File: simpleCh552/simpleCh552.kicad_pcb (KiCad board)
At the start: 2 copper layers, 20 x 27 mm, 15 parts, among them J1 Conn_01x02_Pin, J2 left, J3 Conn_01x03_Pin, SW1 SW_SPST, U1 CH552G

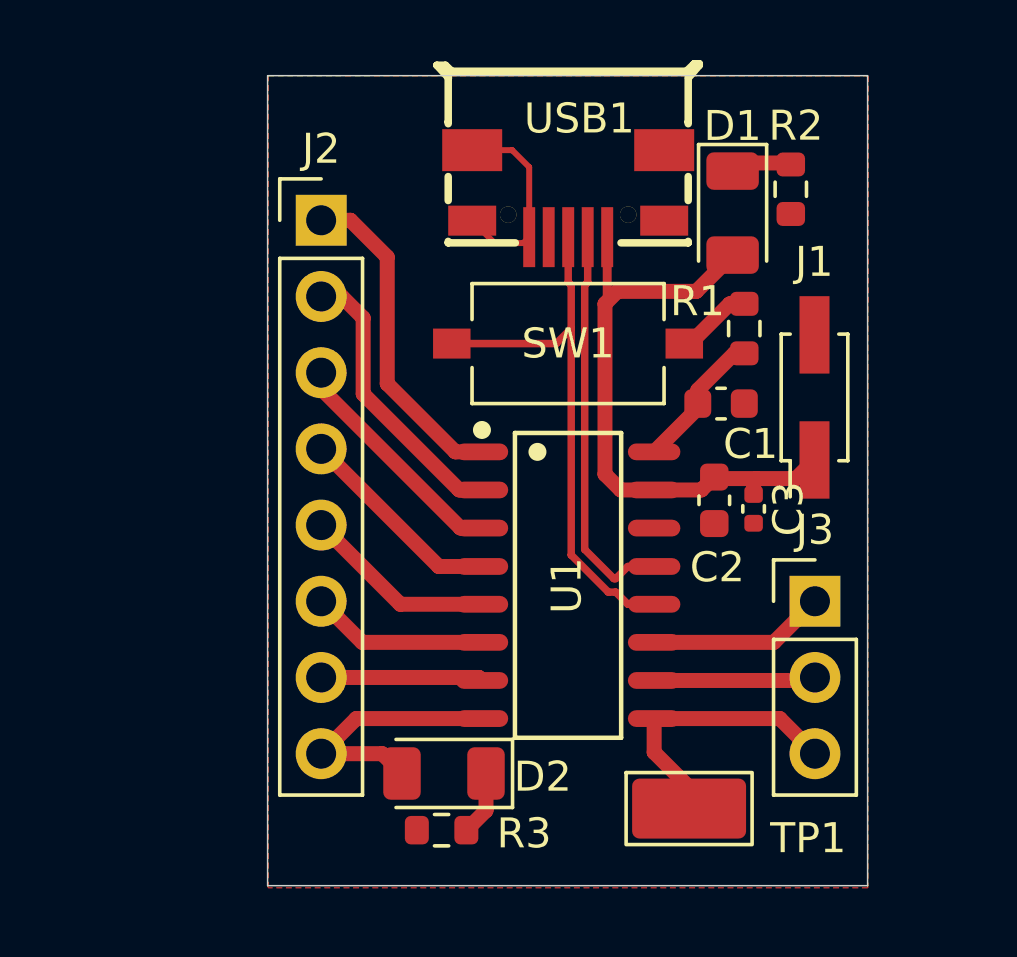
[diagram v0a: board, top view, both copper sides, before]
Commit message: Updated with MicroUSB link
Microsub board ready V1
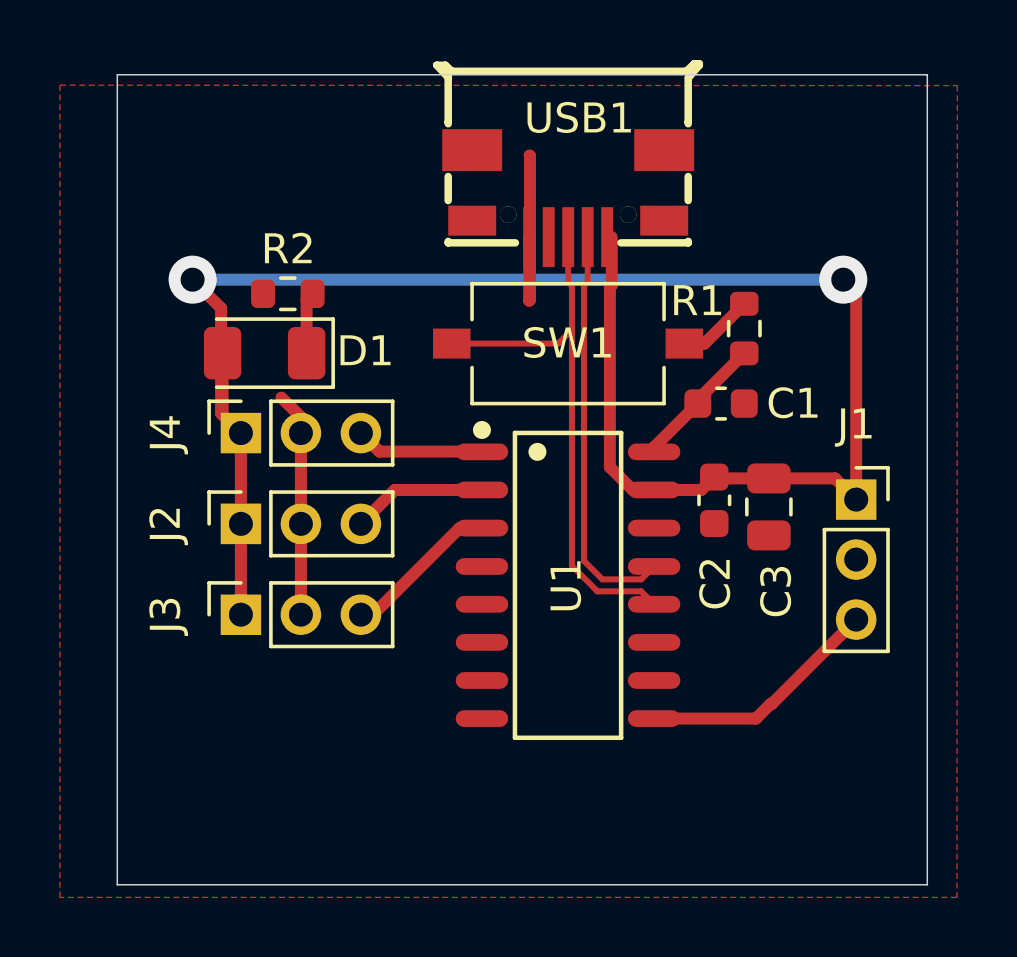
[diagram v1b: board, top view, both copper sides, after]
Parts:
- removed D2: LED, LED_SMD:LED_1206_3216Metric
- removed R3: 1k, Resistor_SMD:R_0603_1608Metric
- removed TP1: TestPoint, TestPoint:TestPoint_Keystone_5019_Miniature
- added J4: A3, Connector_PinSocket_2.00mm:PinSocket_1x03_P2.00mm_Vertical, F.Cu at (132.2, 60.0)
- C3: value 100n -> 10uf; footprint Capacitor_SMD:C_0402_1005Metric -> Capacitor_SMD:C_0805_2012Metric
- J1: value Conn_01x02_Pin -> A0; footprint Connector_PinHeader_2.00mm:PinHeader_2x01_P2.00mm_Vertical_SMD -> Connector_PinSocket_2.00mm:PinSocket_1x03_P2.00mm_Vertical
- J2: value left -> A1; footprint Connector_PinHeader_2.54mm:PinHeader_1x08_P2.54mm_Vertical -> Connector_PinSocket_2.00mm:PinSocket_1x03_P2.00mm_Vertical
- J3: value Conn_01x03_Pin -> A2; footprint Connector_PinHeader_2.54mm:PinHeader_1x03_P2.54mm_Vertical -> Connector_PinSocket_2.00mm:PinSocket_1x03_P2.00mm_Vertical
- moved J3 19.1 mm to (132.2, 66.0), turned to 90 degrees
- moved R2 17.1 mm to (133.8, 55.3), turned to 180 degrees
- moved D1 16.3 mm to (133.0, 57.3), turned to 180 degrees
- moved J2 10.5 mm to (132.2, 63.0), turned to 90 degrees
- moved J1 3.68 mm to (152.7, 62.2), turned to 0 degrees
- moved C3 0.51 mm to (149.8, 62.4)
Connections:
- J2 pad 1: Net-(J2-Pin_1) -> VCC
- J2 pad 2: Net-(J2-Pin_2) -> GND
- J2 pad 3: Net-(J2-Pin_3) -> A1
- J3 pad 1: /3.4 -> VCC
- J3 pad 2: /3.2 -> GND
- J3 pad 3: /1.1 -> A2
- U1 pad 1: Net-(J2-Pin_1) -> A3
- U1 pad 2: Net-(J2-Pin_2) -> A1
- U1 pad 3: Net-(J2-Pin_3) -> A2
- U1 pad 4: Net-(J2-Pin_4) -> unconnected-(U1-P1.6/MISO/RXD1/TIN4-Pad4)
- U1 pad 5: Net-(J2-Pin_5) -> unconnected-(U1-P1.7/SCK/TXD1/TIN5-Pad5)
- U1 pad 6: Net-(J2-Pin_6) -> unconnected-(U1-RST/T2EX_/CAP2_-Pad6)
- U1 pad 7: Net-(J2-Pin_7) -> unconnected-(U1-P3.1/PWM2_/TXD-Pad7)
- U1 pad 8: /3.0 -> unconnected-(U1-P3.0/PWM1_/RXD-Pad8)
- U1 pad 9: /1.1 -> A0
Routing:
- net VCC: track 21.1 -> 60.7 mm, vias 0 -> 2
- net Net-(J2-Pin_1): track 11.0 -> 0.00 mm
- net Net-(J2-Pin_2): track 9.51 -> 0.00 mm
- net /1.1: track 9.33 -> 0.00 mm
- net /3.0: track 8.81 -> 0.00 mm
- net A0: track 0.00 -> 8.10 mm
- net GND: track 6.76 -> 14.6 mm
- net Net-(J2-Pin_3): track 7.82 -> 0.00 mm
- net Net-(J2-Pin_4): track 6.98 -> 0.00 mm
- net Net-(J2-Pin_5): track 6.45 -> 0.00 mm
- net Net-(J2-Pin_6): track 5.93 -> 0.00 mm
- net /3.4: track 5.93 -> 0.00 mm
- net Net-(J2-Pin_7): track 5.40 -> 0.00 mm
- net /3.2: track 5.40 -> 0.00 mm
- net A2: track 0.00 -> 5.23 mm
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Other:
- board size 20 x 27 mm -> 27 x 27 mm

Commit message: update
update
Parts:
- removed USB1: MICROQTJ, mylib:MICRO-USB-SMD_MICROQTJ-5P
- added H1: MountingHole, MountingHole:MountingHole_2.1mm, F.Cu at (152.1, 51.3)
- added J5: Conn_01x04, Connector_PinSocket_2.54mm:PinSocket_1x04_P2.54mm_Vertical, F.Cu at (145.9, 52.3)
- R1, R2: footprint Resistor_SMD:R_0603_1608Metric -> Resistor_SMD:R_1206_3216Metric
- moved D1 1.18 mm to (134.2, 57.2)
- moved SW1 1.14 mm to (142.0, 57.1)
- moved R1 0.61 mm to (149.2, 55.9)
- moved R2 0.59 mm to (134.2, 54.9)
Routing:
- net GND: track 14.6 -> 8.51 mm
- net VCC: track 60.7 -> 55.4 mm, vias 2 -> 0
- net /D+: track 18.5 -> 22.0 mm
- net Net-(SW1-B): track 2.55 -> 5.40 mm
- net /D-: track 13.6 -> 15.6 mm
- net +3V3: track 4.53 -> 5.29 mm
- net A0: track 8.10 -> 8.76 mm
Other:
- board text added: "ch552Deej - Ved"

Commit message: update
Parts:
- removed H1: MountingHole, MountingHole:MountingHole_2.1mm
- removed the J1 at (152.7, 62.2)
- J2: value A1 -> Conn_01x04; footprint Connector_PinSocket_2.00mm:PinSocket_1x03_P2.00mm_Vertical -> Connector_Wire:SolderWire-0.5sqmm_1x04_P4.6mm_D0.9mm_OD2.1mm
- J3: value A2 -> Conn_01x04; footprint Connector_PinSocket_2.00mm:PinSocket_1x03_P2.00mm_Vertical -> Connector_Wire:SolderWire-0.5sqmm_1x04_P4.6mm_D0.9mm_OD2.1mm
- J4: value A3 -> Conn_01x04; footprint Connector_PinSocket_2.00mm:PinSocket_1x03_P2.00mm_Vertical -> Connector_Wire:SolderWire-0.5sqmm_1x04_P4.6mm_D0.9mm_OD2.1mm
- moved R1 23.4 mm to (149.0, 73.0), turned to -90 degrees
- moved J4 22.0 mm to (153.5, 65.5)
- moved D1 18.4 mm to (149.0, 68.1), turned to 90 degrees
- moved J2 15.4 mm to (143.0, 74.0), turned to 180 degrees
- moved J3 2.71 mm to (129.6, 65.5)
- moved J1 1.10 mm to (146.9, 51.8)
- moved C1 1.00 mm to (148.9, 59.7)
- moved R2 0.65 mm to (148.6, 56.1)
- moved C3 0.62 mm to (150.4, 62.4)
- moved SW1 0.51 mm to (142.0, 56.6)
- moved C2 0.23 mm to (148.0, 62.5)
- renumbered J5 to J1, R2 to R1, R1 to R2
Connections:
- J2 pad 1: VCC -> A0
- J2 pad 2: GND -> A2
- J3 pad 1: VCC -> GND
- J3 pad 3: A2 -> GND
- J4 pad 2: GND -> VCC
- J4 pad 3: A3 -> VCC
- U1 pad 10: /3.2 -> unconnected-(U1-P3.3/INT1-Pad10)
- U1 pad 11: /3.4 -> unconnected-(U1-P3.4/PWM2/RXD1_/T0-Pad11)
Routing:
- net VCC: track 55.4 -> 33.3 mm
- net A3: track 4.29 -> 20.2 mm
- net A1: track 4.50 -> 16.0 mm
- net GND: track 8.51 -> 0.00 mm
- net A2: track 5.23 -> 12.3 mm
- net A0: track 8.76 -> 6.64 mm
- net Net-(SW1-B): track 5.40 -> 3.79 mm
- net /D+: track 22.0 -> 21.0 mm
- net /D-: track 15.6 -> 14.9 mm
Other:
- board size 27 x 27 mm -> 30 x 30 mm
- board text added: "ch552Deej By Ved"
- board text removed: "ch552Deej - Ved"

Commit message: updated with pot
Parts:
- removed J2, J3, J4: Conn_01x04, Connector_Wire:SolderWire-0.5sqmm_1x04_P4.6mm_D0.9mm_OD2.1mm
- added J5: Conn_01x06, Connector_Wire:SolderWire-0.1sqmm_1x06_P3.6mm_D0.4mm_OD1mm, B.Cu at (93.6, 63.5)
- added J6: Conn_01x06, Connector_Wire:SolderWire-0.1sqmm_1x06_P3.6mm_D0.4mm_OD1mm, F.Cu at (166.8, 75.0)
- added RV1: pot1, Potentiometer_THT:Potentiometer_Omeg_PC16BU_Vertical, F.Cu at (93.2, 47.1)
- added RV2: pot1, Potentiometer_THT:Potentiometer_Omeg_PC16BU_Vertical, F.Cu at (115.4, 54.1)
- added RV3: pot1, Potentiometer_THT:Potentiometer_Omeg_PC16BU_Vertical, F.Cu at (86.2, 69.5)
- added RV4: pot1, Potentiometer_THT:Potentiometer_Omeg_PC16BU_Vertical, F.Cu at (108.3, 76.6)
- moved R1 34.8 mm to (183.8, 71.2), turned to 0 degrees
- moved D1 34.8 mm to (183.8, 68.6), turned to 0 degrees
- moved C1 33.5 mm to (182.4, 61.2)
- moved C2 33.5 mm to (181.5, 63.9)
- moved C3 33.5 mm to (183.9, 63.8)
- moved J1 33.5 mm to (180.4, 53.2)
- moved R2 33.5 mm to (182.1, 57.5)
- moved SW1 33.5 mm to (175.5, 58.0)
- moved U1 33.5 mm to (176.6, 66.5)
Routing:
- net VSS: track 0.00 -> 104.9 mm
- net Net-(J5-Pin_4): track 0.00 -> 19.6 mm
- net Net-(J5-Pin_3): track 0.00 -> 19.4 mm
- net Net-(J5-Pin_2): track 0.00 -> 16.0 mm
- net Net-(J5-Pin_5): track 0.00 -> 11.2 mm
- net A3: track 20.2 -> 15.0 mm
- net VCC: track 33.3 -> 37.6 mm
- net A2: track 12.3 -> 15.9 mm
- net A0: track 6.64 -> 4.77 mm
- net A1: track 16.0 -> 15.1 mm
- net Net-(D1-K): track 2.06 -> 2.60 mm
- added copper zone on F.Cu, net GND1
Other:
- board size 30 x 30 mm -> 109.3 x 40 mm
- board text added: "ch552Deej By Ved Made In India"
- board text removed: "ch552Deej By Ved"
